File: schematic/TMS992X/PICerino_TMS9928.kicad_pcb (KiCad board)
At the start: 2 copper layers, 105.2 x 112.5 mm, 75 parts, among them CON1 PICERINO-EDGE, J1 Conn_01x02, J10 Conn_01x03, J2 Conn_01x03, J3 Conn_01x03, J4 Conn_01x03, J5 Y, J6 Yr, J7 Yb, J8 Conn_01x08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

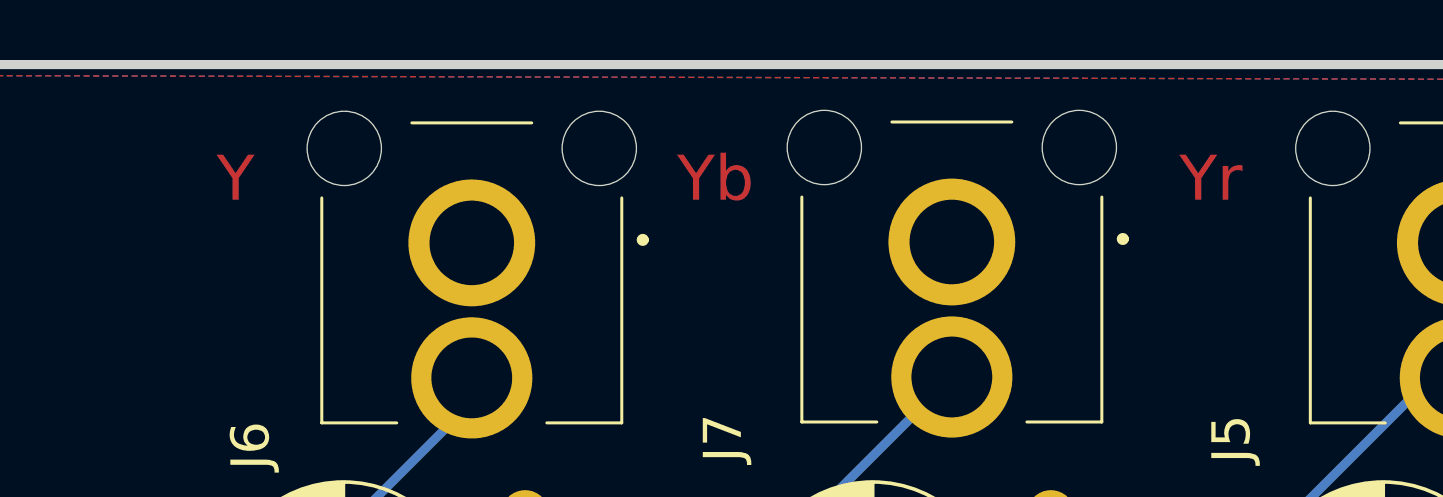
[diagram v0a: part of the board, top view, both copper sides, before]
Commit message: added new switch and sample video chip to simplify video output. work in progress.
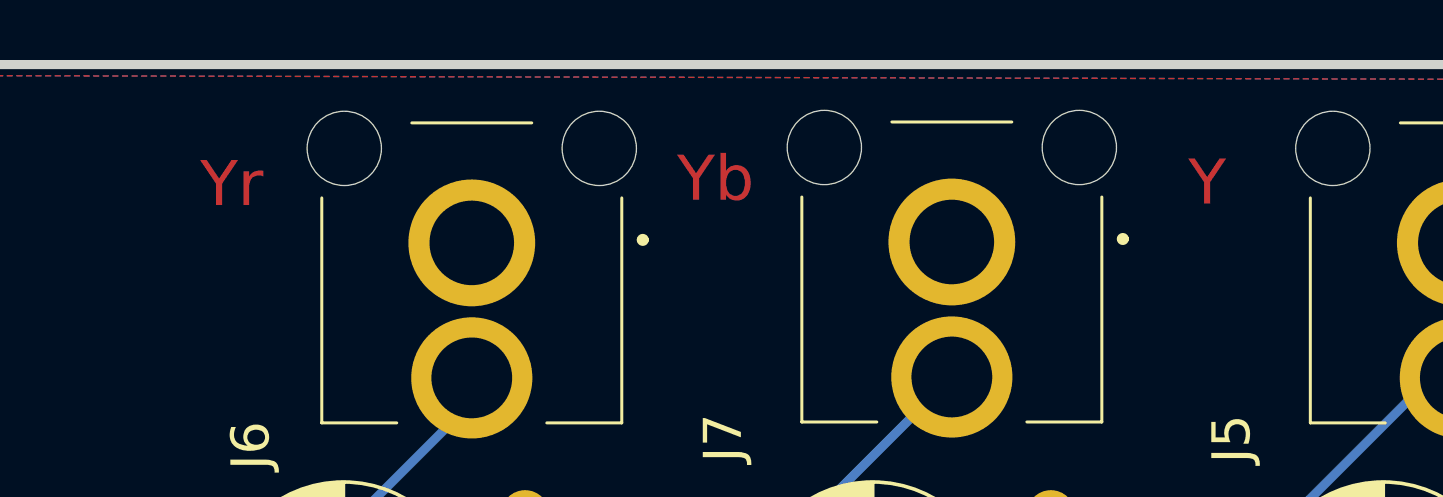
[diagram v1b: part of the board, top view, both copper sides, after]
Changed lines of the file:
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@@
     (40 "Dwgs.User" user "User.Drawings")
     (41 "Cmts.User" user "User.Comments")
-    (42 "Eco1.User" user "User.Eco1")
+    (42 "Eco1.User" user "Edge.Cuts.Mill")
     (43 "Eco2.User" user "User.Eco2")
     (44 "Edge.Cuts" user)
@@
     (pad_to_mask_clearance 0)
     (pcbplotparams
-      (layerselection 0x0001000_fffffffe)
+      (layerselection 0x0000400_ffffffff)
       (plot_on_all_layers_selection 0x0000000_00000000)
       (disableapertmacros false)
@@
     )
   )
+  (gr_line (start 105.7148 34.8742) (end 105.7402 128.9304)
+    (stroke (width 0.79375) (type default)) (layer "Eco1.User"))
+  (gr_line (start 196.088 153.1874) (end 196.088 137.3886)
+    (stroke (width 0.79375) (type default)) (layer "Eco1.User"))
+  (gr_line (start 113.2586 154.6098) (end 194.691 154.6098)
+    (stroke (width 0.79375) (type default)) (layer "Eco1.User"))
+  (gr_line (start 211.3788 33.1978) (end 210.9978 33.1978)
+    (stroke (width 0.79375) (type default)) (layer "Eco1.User"))
+  (gr_line (start 194.691 154.6098) (end 196.088 153.1874)
+    (stroke (width 0.79375) (type default)) (layer "Eco1.User"))
+  (gr_line (start 211.4296 122.3518) (end 211.3788 34.7472)
+    (stroke (width 0.79375) (type default)) (layer "Eco1.User"))
+  (gr_line (start 105.7402 128.9304) (end 111.7092 137.5664)
+    (stroke (width 0.79375) (type default)) (layer "Eco1.User"))
+  (gr_line (start 111.7092 137.5664) (end 111.7092 153.289)
+    (stroke (width 0.79375) (type default)) (layer "Eco1.User"))
+  (gr_line (start 210.9978 33.1978) (end 105.7148 33.2232)
+    (stroke (width 0.79375) (type default)) (layer "Eco1.User"))
+  (gr_line (start 196.088 137.3886) (end 211.4296 122.3518)
+    (stroke (width 0.79375) (type default)) (layer "Eco1.User"))
+  (gr_line (start 111.7092 153.289) (end 113.2586 154.6098)
+    (stroke (width 0.79375) (type default)) (layer "Eco1.User"))
   (gr_line (start 211.074 33.528) (end 211.074 49.53)
     (stroke (width 0.3048) (type solid)) (layer "Edge.Cuts"))
@@
     (effects (font (size 1.5 1.5) (thickness 0.3302)))
   )
-  (gr_text "Yr" (at 194.31 37.338) (layer "F.Cu")
+  (gr_text "Yr" (at 161.671 37.5158) (layer "F.Cu")
     (effects (font (size 1.5 1.5) (thickness 0.3)))
   )
@@
     (effects (font (size 1.5 1.5) (thickness 0.3)))
   )
-  (gr_text "Y" (at 161.798 37.338) (layer "F.Cu")
+  (gr_text "Y" (at 194.183 37.465) (layer "F.Cu")
     (effects (font (size 1.5 1.5) (thickness 0.3)))
   )

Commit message: initial commit of v2 tms992X board
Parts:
- removed C10: 20pf, Capacitor_THT:C_Rect_L10.0mm_W5.0mm_P5.00mm_P7.50mm
- removed C22, C29, C30: 470uF, Capacitor_THT:CP_Radial_D8.0mm_P5.00mm
- removed C23: 100nF, Capacitor_THT:C_Disc_D4.7mm_W2.5mm_P5.00mm
- removed C26: 220pf, Capacitor_THT:C_Disc_D4.7mm_W2.5mm_P5.00mm
- removed D1: D_Schottky, Diode_THT:D_DO-35_SOD27_P7.62mm_Horizontal
- removed R11: 1K, Resistor_THT:R_Axial_DIN0207_L6.3mm_D2.5mm_P7.62mm_Horizontal
- removed R12: 510R, Resistor_THT:R_Axial_DIN0207_L6.3mm_D2.5mm_P7.62mm_Horizontal
- removed TP2: TestPoint, Connector_PinHeader_2.54mm:PinHeader_1x01_P2.54mm_Vertical
- removed U4: NE5532, Package_DIP:DIP-8_W7.62mm_LongPads
- removed U7: ADG453, Package_DIP:DIP-16_W7.62mm_LongPads
- added R3: 1M, Resistor_THT:R_Axial_DIN0207_L6.3mm_D2.5mm_P7.62mm_Horizontal, F.Cu at (192.8, 103.2)
- added U14: MAX333, Package_DIP:DIP-20_W7.62mm_LongPads, F.Cu at (178.8, 90.5)
- C11: value 18pF -> 33pF
- R1: value 10K -> 4k7
- R2: value 510R -> 4k7
- moved C3 50.6 mm to (140.5, 60.0), turned to -90 degrees
- moved TP1 20.1 mm to (193.8, 96.5)
- moved C4 8.10 mm to (189.5, 101.0), turned to 90 degrees
- moved C18 4.09 mm to (198.4, 112.6)
- moved C11 3.17 mm to (177.3, 136.4), turned to 180 degrees
- moved R2 1.64 mm to (196.0, 107.2)
- moved C25 1.53 mm to (189.6, 113.3), turned to 90 degrees
- moved U1 1.45 mm to (199.1, 107.2)
- moved C5 0.55 mm to (197.5, 96.6), turned to 90 degrees
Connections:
- C25 pad 1: Net-(U4A-+) -> VSS
- C25 pad 2: VSS -> Net-(C25-Pad2)
- J5 pad T: Net-(C22-Pad2) -> Net-(J5-PadT)
- J6 pad T: Net-(C29-Pad2) -> Net-(J6-PadT)
- J7 pad T: Net-(C30-Pad2) -> Net-(J7-PadT)
- R17 pad 1: Net-(C29-Pad1) -> Net-(J6-PadT)
- R18 pad 1: Net-(C30-Pad1) -> Net-(J7-PadT)
- R2 pad 1: Net-(U7-IN1) -> Net-(U1-CSYNC)
- R2 pad 2: Net-(U4B--) -> VCC
- R8 pad 1: Net-(C22-Pad1) -> Net-(J5-PadT)
- TP1 pad 1: Net-(U7-IN1) -> Net-(U1-BURST)
- U1 pad 1: unconnected-(U1-CSYNC-Pad1) -> Net-(U1-CSYNC)
- U2 pad 1: unconnected-(U2A-~{DISABLE}-Pad1) -> VCC
- U2 pad 2: unconnected-(U2B-~{DISABLE}-Pad2) -> VCC
- U2 pad 3: unconnected-(U2C-~{DISABLE}-Pad3) -> VCC
- U2 pad 5: Net-(J2-Pin_2) -> Net-(U2A-+)
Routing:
- net Net-(U7-IN1): track 68.1 -> 0.00 mm
- net Net-(J2-Pin_2): track 82.1 -> 26.1 mm
- net Net-(U1-BURST): track 20.8 -> 67.0 mm
- net Net-(J3-Pin_2): track 54.6 -> 19.6 mm
- net Net-(D1-K): track 30.8 -> 0.00 mm
- net Net-(U2A-+): track 0.00 -> 25.6 mm
- net Net-(U2B-+): track 30.4 -> 55.8 mm
- net Net-(C25-Pad2): track 0.00 -> 20.8 mm
- net Net-(U1-CSYNC): track 0.00 -> 17.6 mm
- net Net-(J4-Pin_2): track 64.0 -> 49.8 mm
- net Net-(U4A--): track 13.8 -> 0.00 mm
- net Net-(U2C-+): track 31.4 -> 44.9 mm
- net Net-(C29-Pad2): track 10.4 -> 0.00 mm
- net Net-(C22-Pad2): track 10.3 -> 0.00 mm
- net Net-(C30-Pad2): track 9.75 -> 0.00 mm
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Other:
- board text added: "2023 JAY CONVERTINO TMS992X TEST BOARD V2"
- board text removed: "2023 JAY CONVERTINO TMS992X TEST BOARD V1"
